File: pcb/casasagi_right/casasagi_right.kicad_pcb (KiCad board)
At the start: 2 copper layers, 133.3 x 82.7 mm, 114 parts, among them J201 USB_C_Receptacle_USB2.0, J202 AudioJack4, J203 Conn_01x05, SW201 RESET, SW202 BOOT, U201 TLV73333PDBV, U202 AT24CS32-XHM, U203 STM32F072C8Tx, Y201 8MHz

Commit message: add logo!!!!
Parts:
- added LOGO1: casasagi_logo, casasagi:logo, B.Cu at (58.5, 82.2)

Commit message: add combined pcb
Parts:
- moved J203 4.50 mm to (128.8, 42.0)
- moved R209 0.50 mm to (114.2, 49.5)
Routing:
- net +3V3: track 125.4 -> 120.5 mm
- net /RESET: track 56.8 -> 54.9 mm
- net /SWDIO: track 37.7 -> 35.9 mm
- net Net-(R209-Pad1): track 8.34 -> 7.74 mm
- net GND: vias 138 -> 141

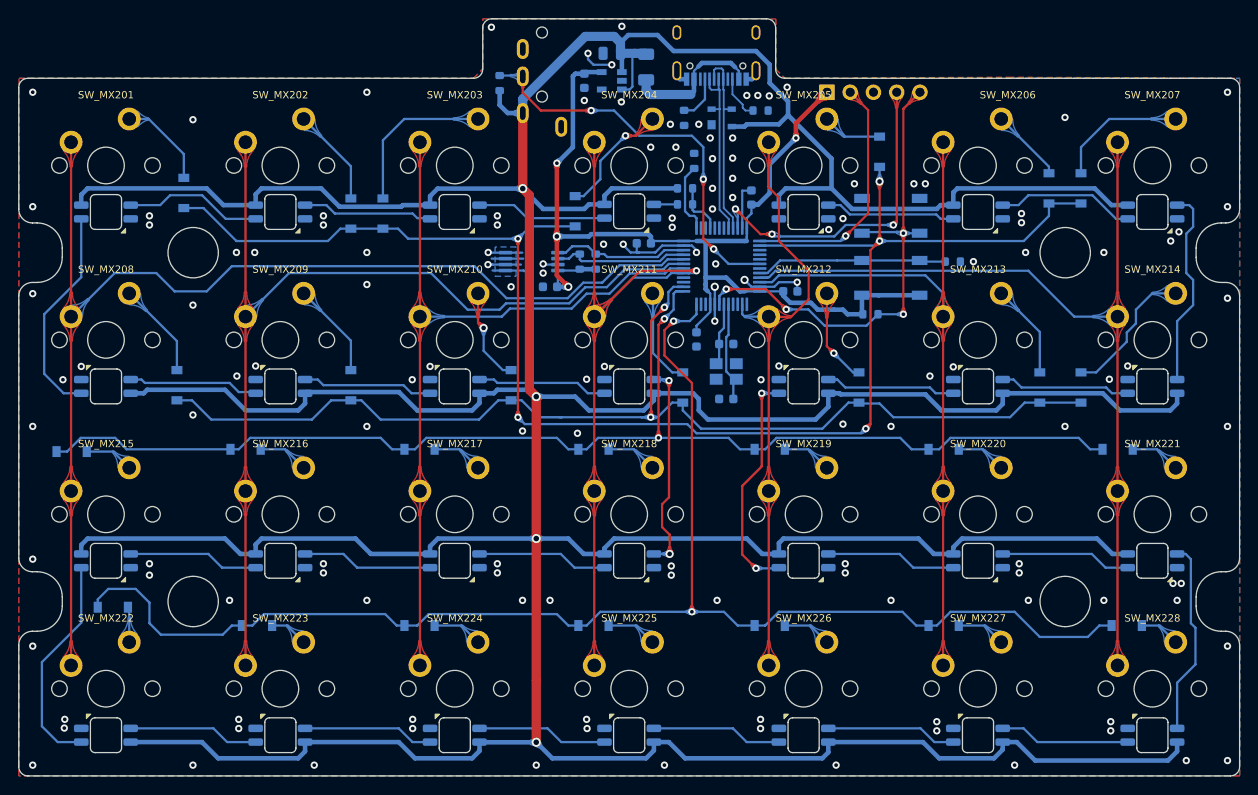
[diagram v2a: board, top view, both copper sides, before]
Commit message: prepare pcb for BOM and add BOM left
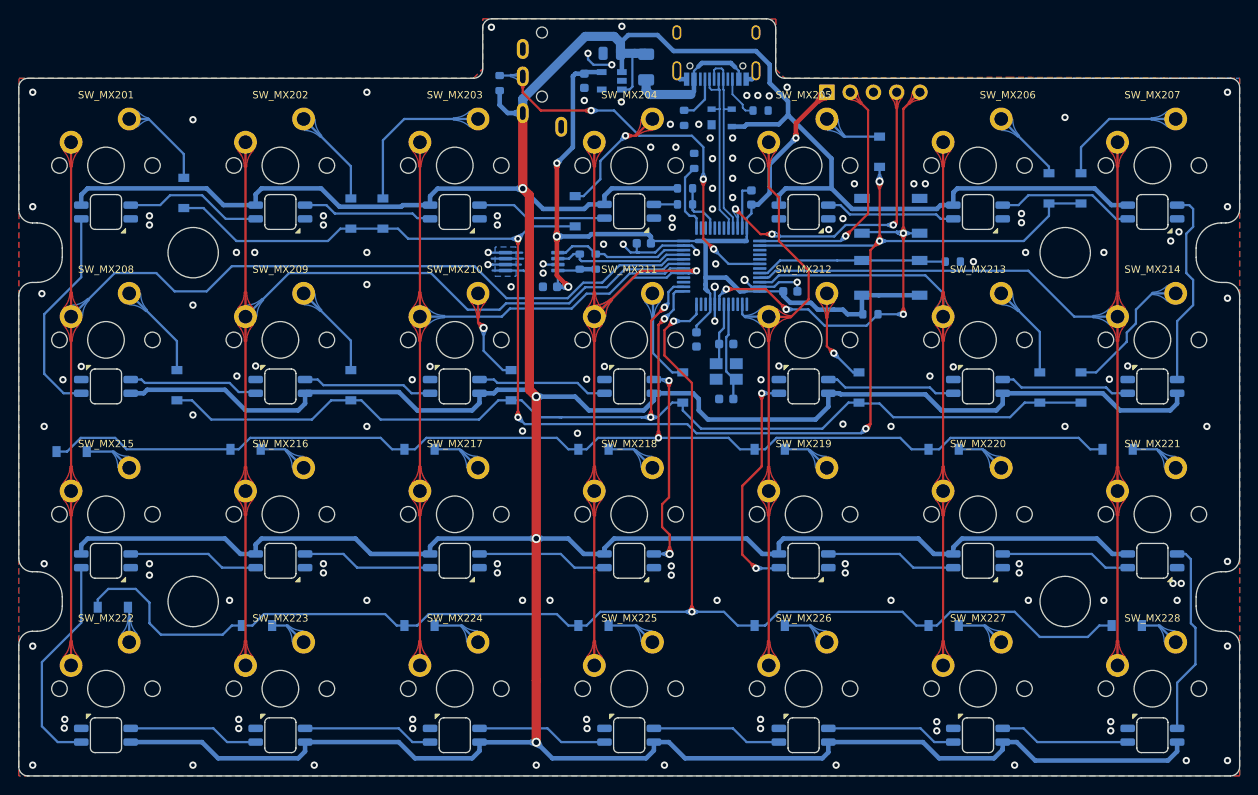
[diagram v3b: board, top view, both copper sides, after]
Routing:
- net GND: vias 141 -> 142

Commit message: Change boss thru hole to M2 thru hole
Introduce M2 thru hole to fix switch plate and PCB together using M2 screw. Spacer style boss can be placed at the edge cutout.
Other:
- outline, holes or cut-outs redrawn

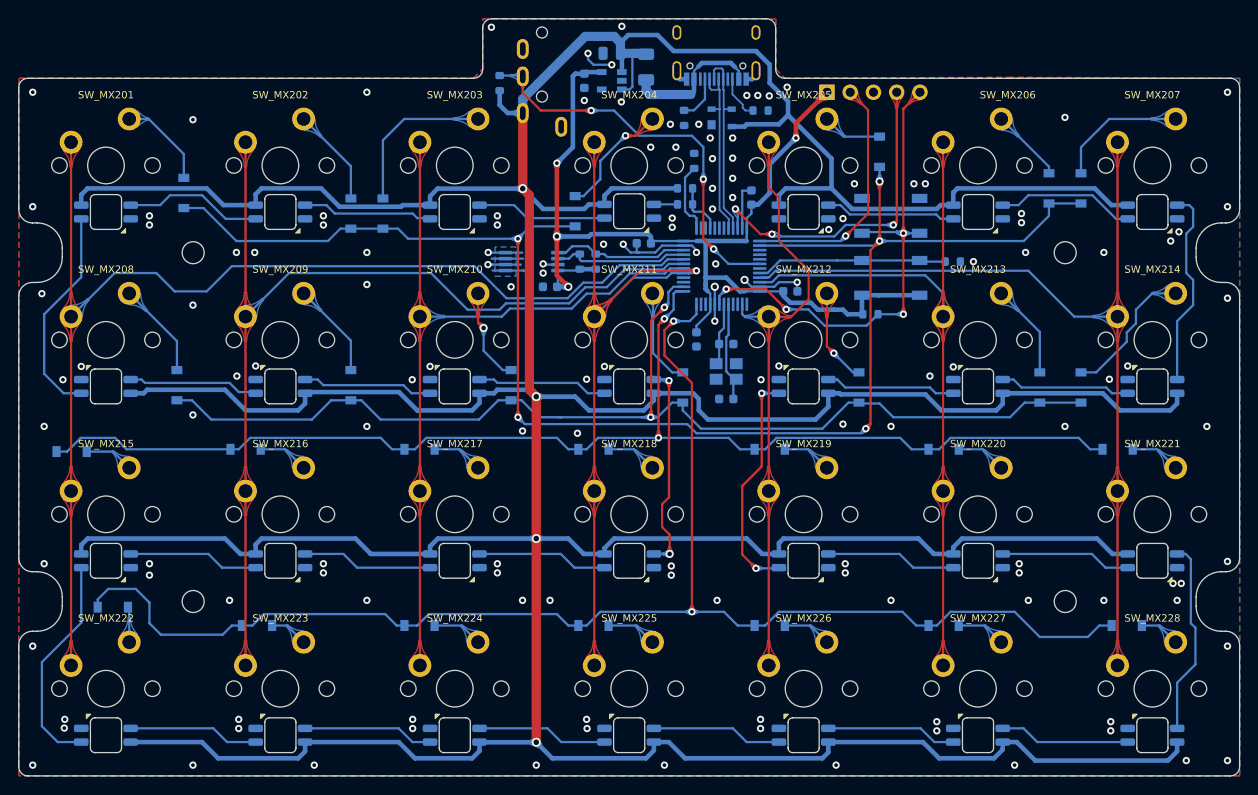
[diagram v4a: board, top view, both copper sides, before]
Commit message: replace M2 holes to drill holes
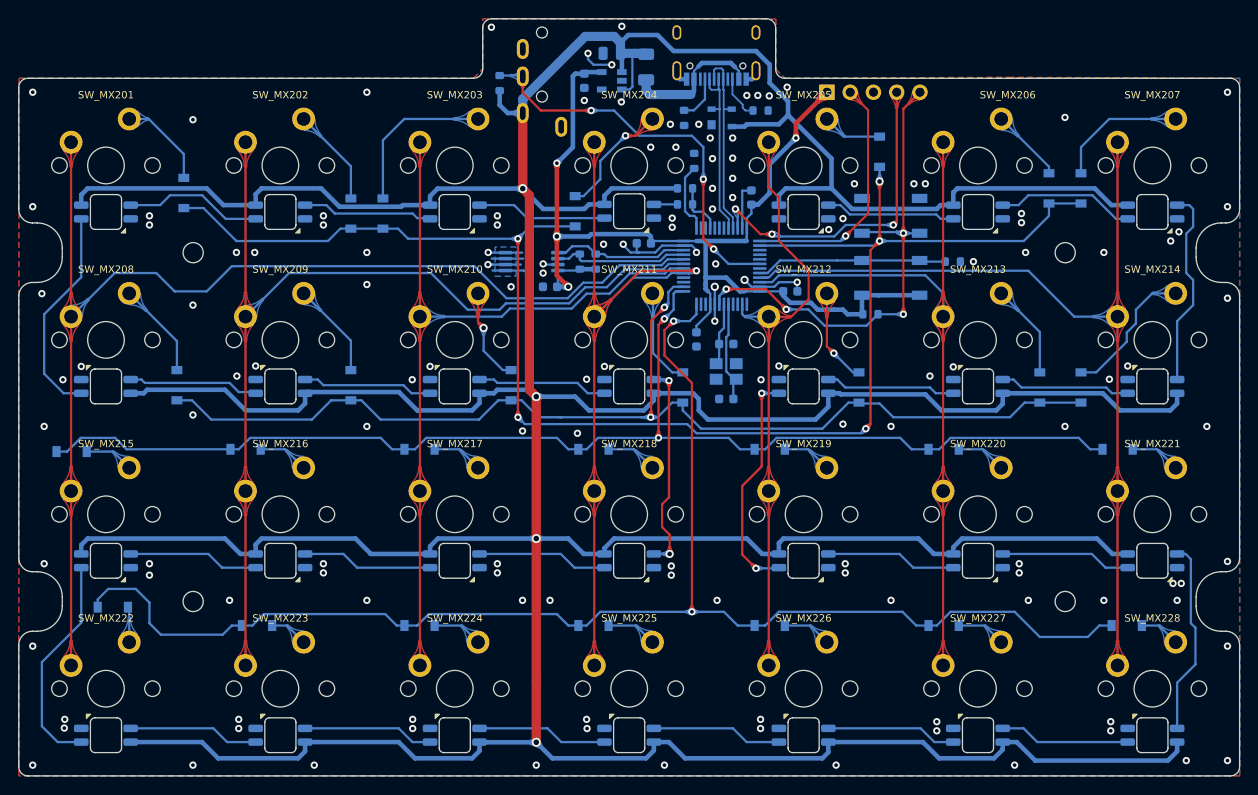
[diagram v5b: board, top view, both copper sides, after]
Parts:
- added H1: M2, MountingHole:MountingHole_2.2mm_M2, F.Cu at (59.5, 59.5)
- added H2: M2, MountingHole:MountingHole_2.2mm_M2, F.Cu at (59.5, 97.6)
- added H3: M2, MountingHole:MountingHole_2.2mm_M2, F.Cu at (154.8, 59.5)
- added H4: M2, MountingHole:MountingHole_2.2mm_M2, F.Cu at (154.8, 97.6)
- U202: value AT24CS32-XHM -> AT24C256C-XHL-T
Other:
- outline, holes or cut-outs redrawn
